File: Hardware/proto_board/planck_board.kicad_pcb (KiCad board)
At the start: 2 copper layers, 80.8 x 60.1 mm, 1 part, among them J1 Conn_01x40

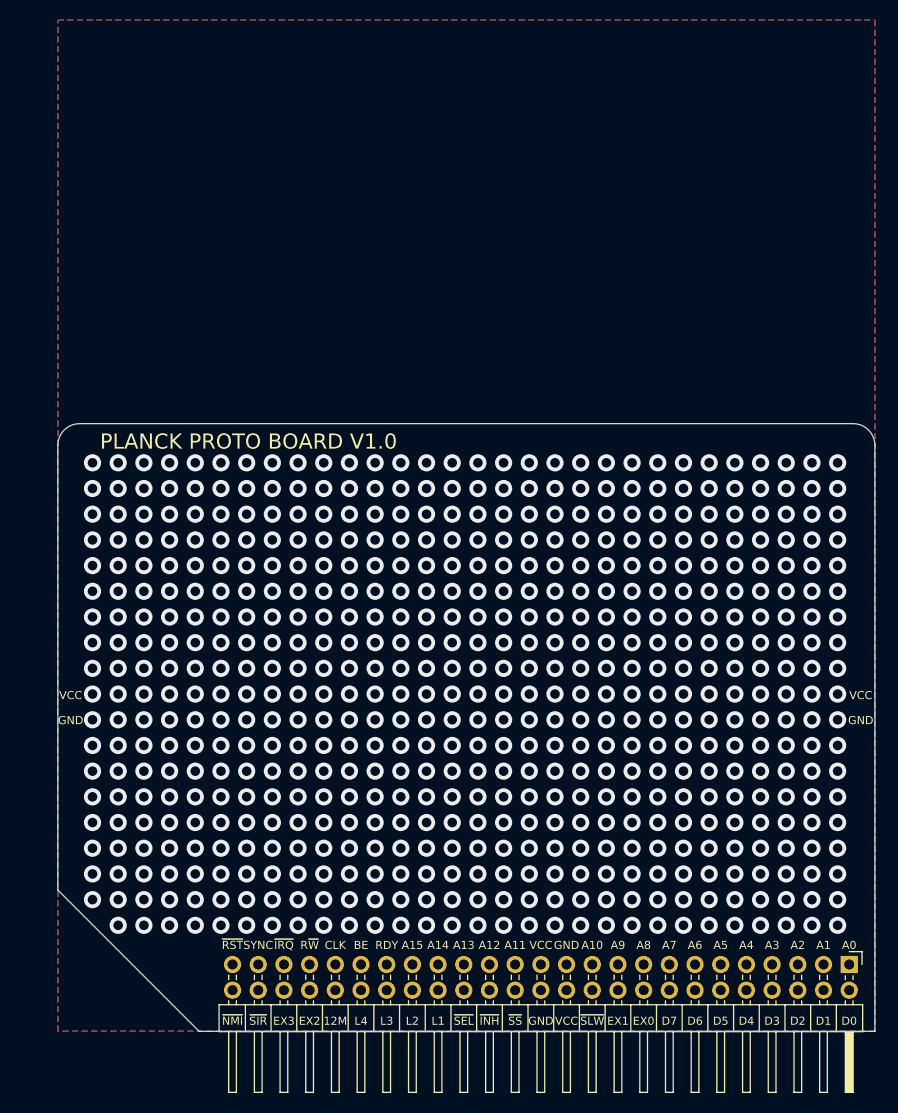
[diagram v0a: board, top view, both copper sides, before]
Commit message: update with proper pin holes
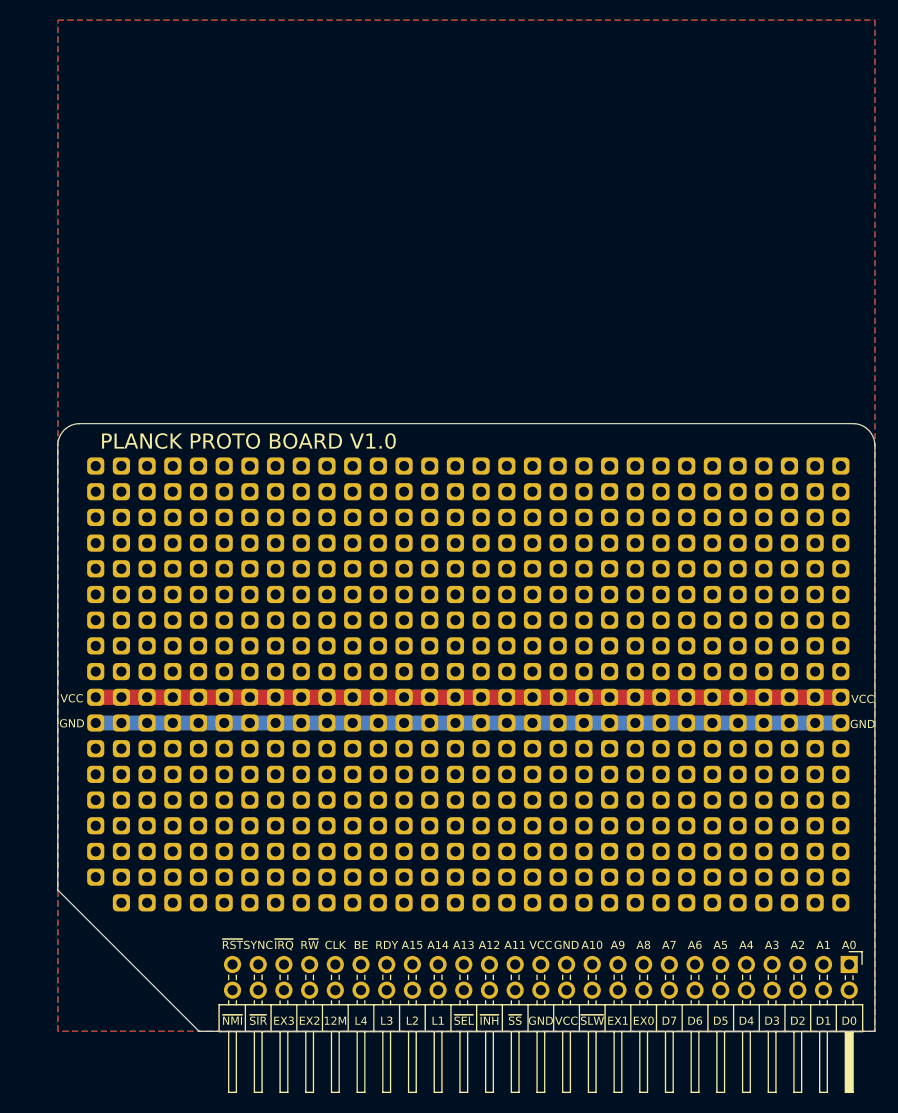
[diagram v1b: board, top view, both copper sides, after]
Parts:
- added REF**: PinHole, Connector_PinHeader_2.54mm:PinHole, F.Cu at (77.4, -33.0)
- added REF**: PinHole, Connector_PinHeader_2.54mm:PinHole, F.Cu at (54.5, -33.0)
- added REF**: PinHole, Connector_PinHeader_2.54mm:PinHole, F.Cu at (46.9, -17.8)
- added REF**: PinHole, Connector_PinHeader_2.54mm:PinHole, F.Cu at (44.4, -17.8)
- added REF**: PinHole, Connector_PinHeader_2.54mm:PinHole, F.Cu at (41.8, -17.8)
- added REF**: PinHole, Connector_PinHeader_2.54mm:PinHole, F.Cu at (39.3, -17.8)
- added REF**: PinHole, Connector_PinHeader_2.54mm:PinHole, F.Cu at (36.8, -17.8)
- added REF**: PinHole, Connector_PinHeader_2.54mm:PinHole, F.Cu at (34.2, -17.8)
- added REF**: PinHole, Connector_PinHeader_2.54mm:PinHole, F.Cu at (31.7, -17.8)
- added REF**: PinHole, Connector_PinHeader_2.54mm:PinHole, F.Cu at (29.1, -17.8)
- added REF**: PinHole, Connector_PinHeader_2.54mm:PinHole, F.Cu at (26.6, -17.8)
- added REF**: PinHole, Connector_PinHeader_2.54mm:PinHole, F.Cu at (24.1, -17.8)
- added REF**: PinHole, Connector_PinHeader_2.54mm:PinHole, F.Cu at (52.0, -33.0)
- added REF**: PinHole, Connector_PinHeader_2.54mm:PinHole, F.Cu at (21.5, -17.8)
- added REF**: PinHole, Connector_PinHeader_2.54mm:PinHole, F.Cu at (19.0, -17.8)
- added REF**: PinHole, Connector_PinHeader_2.54mm:PinHole, F.Cu at (16.4, -17.8)
- added REF**: PinHole, Connector_PinHeader_2.54mm:PinHole, F.Cu at (13.9, -17.8)
- added REF**: PinHole, Connector_PinHeader_2.54mm:PinHole, F.Cu at (11.4, -17.8)
- added REF**: PinHole, Connector_PinHeader_2.54mm:PinHole, F.Cu at (8.83, -17.8)
- added REF**: PinHole, Connector_PinHeader_2.54mm:PinHole, F.Cu at (6.29, -17.8)
- added REF**: PinHole, Connector_PinHeader_2.54mm:PinHole, F.Cu at (3.75, -17.8)
- added REF**: PinHole, Connector_PinHeader_2.54mm:PinHole, F.Cu at (77.4, -20.3)
- added REF**: PinHole, Connector_PinHeader_2.54mm:PinHole, F.Cu at (74.9, -20.3)
- added REF**: PinHole, Connector_PinHeader_2.54mm:PinHole, F.Cu at (49.5, -33.0)
- added REF**: PinHole, Connector_PinHeader_2.54mm:PinHole, F.Cu at (72.3, -20.3)
- added REF**: PinHole, Connector_PinHeader_2.54mm:PinHole, F.Cu at (69.8, -20.3)
- added REF**: PinHole, Connector_PinHeader_2.54mm:PinHole, F.Cu at (67.2, -20.3)
- added REF**: PinHole, Connector_PinHeader_2.54mm:PinHole, F.Cu at (64.7, -20.3)
- added REF**: PinHole, Connector_PinHeader_2.54mm:PinHole, F.Cu at (62.2, -20.3)
- added REF**: PinHole, Connector_PinHeader_2.54mm:PinHole, F.Cu at (59.6, -20.3)
- added REF**: PinHole, Connector_PinHeader_2.54mm:PinHole, F.Cu at (57.1, -20.3)
- added REF**: PinHole, Connector_PinHeader_2.54mm:PinHole, F.Cu at (54.5, -20.3)
- added REF**: PinHole, Connector_PinHeader_2.54mm:PinHole, F.Cu at (52.0, -20.3)
- added REF**: PinHole, Connector_PinHeader_2.54mm:PinHole, F.Cu at (49.5, -20.3)
- added REF**: PinHole, Connector_PinHeader_2.54mm:PinHole, F.Cu at (46.9, -33.0)
- added REF**: PinHole, Connector_PinHeader_2.54mm:PinHole, F.Cu at (46.9, -20.3)
- added REF**: PinHole, Connector_PinHeader_2.54mm:PinHole, F.Cu at (44.4, -20.3)
- added REF**: PinHole, Connector_PinHeader_2.54mm:PinHole, F.Cu at (41.8, -20.3)
- added REF**: PinHole, Connector_PinHeader_2.54mm:PinHole, F.Cu at (39.3, -20.3)
- added REF**: PinHole, Connector_PinHeader_2.54mm:PinHole, F.Cu at (36.8, -20.3)
- added REF**: PinHole, Connector_PinHeader_2.54mm:PinHole, F.Cu at (34.2, -20.3)
- added REF**: PinHole, Connector_PinHeader_2.54mm:PinHole, F.Cu at (31.7, -20.3)
- added REF**: PinHole, Connector_PinHeader_2.54mm:PinHole, F.Cu at (29.1, -20.3)
- added REF**: PinHole, Connector_PinHeader_2.54mm:PinHole, F.Cu at (26.6, -20.3)
- added REF**: PinHole, Connector_PinHeader_2.54mm:PinHole, F.Cu at (24.1, -20.3)
- added REF**: PinHole, Connector_PinHeader_2.54mm:PinHole, F.Cu at (44.4, -33.0)
- added REF**: PinHole, Connector_PinHeader_2.54mm:PinHole, F.Cu at (21.5, -20.3)
- added REF**: PinHole, Connector_PinHeader_2.54mm:PinHole, F.Cu at (19.0, -20.3)
- added REF**: PinHole, Connector_PinHeader_2.54mm:PinHole, F.Cu at (16.4, -20.3)
- added REF**: PinHole, Connector_PinHeader_2.54mm:PinHole, F.Cu at (13.9, -20.3)
- added REF**: PinHole, Connector_PinHeader_2.54mm:PinHole, F.Cu at (11.4, -20.3)
- added REF**: PinHole, Connector_PinHeader_2.54mm:PinHole, F.Cu at (8.83, -20.3)
- added REF**: PinHole, Connector_PinHeader_2.54mm:PinHole, F.Cu at (6.29, -20.3)
- added REF**: PinHole, Connector_PinHeader_2.54mm:PinHole, F.Cu at (3.75, -20.3)
- added REF**: PinHole, Connector_PinHeader_2.54mm:PinHole, F.Cu at (77.4, -22.9)
- added REF**: PinHole, Connector_PinHeader_2.54mm:PinHole, F.Cu at (74.9, -22.9)
- added REF**: PinHole, Connector_PinHeader_2.54mm:PinHole, F.Cu at (41.8, -33.0)
- added REF**: PinHole, Connector_PinHeader_2.54mm:PinHole, F.Cu at (72.3, -22.9)
- added REF**: PinHole, Connector_PinHeader_2.54mm:PinHole, F.Cu at (69.8, -22.9)
- added REF**: PinHole, Connector_PinHeader_2.54mm:PinHole, F.Cu at (67.2, -22.9)
- added REF**: PinHole, Connector_PinHeader_2.54mm:PinHole, F.Cu at (64.7, -22.9)
- added REF**: PinHole, Connector_PinHeader_2.54mm:PinHole, F.Cu at (62.2, -22.9)
- added REF**: PinHole, Connector_PinHeader_2.54mm:PinHole, F.Cu at (59.6, -22.9)
- added REF**: PinHole, Connector_PinHeader_2.54mm:PinHole, F.Cu at (57.1, -22.9)
- added REF**: PinHole, Connector_PinHeader_2.54mm:PinHole, F.Cu at (54.5, -22.9)
- added REF**: PinHole, Connector_PinHeader_2.54mm:PinHole, F.Cu at (52.0, -22.9)
- added REF**: PinHole, Connector_PinHeader_2.54mm:PinHole, F.Cu at (49.5, -22.9)
- added REF**: PinHole, Connector_PinHeader_2.54mm:PinHole, F.Cu at (39.3, -33.0)
- added REF**: PinHole, Connector_PinHeader_2.54mm:PinHole, F.Cu at (46.9, -22.9)
- added REF**: PinHole, Connector_PinHeader_2.54mm:PinHole, F.Cu at (44.4, -22.9)
- added REF**: PinHole, Connector_PinHeader_2.54mm:PinHole, F.Cu at (41.8, -22.9)
- added REF**: PinHole, Connector_PinHeader_2.54mm:PinHole, F.Cu at (39.3, -22.9)
- added REF**: PinHole, Connector_PinHeader_2.54mm:PinHole, F.Cu at (36.8, -22.9)
- added REF**: PinHole, Connector_PinHeader_2.54mm:PinHole, F.Cu at (34.2, -22.9)
- added REF**: PinHole, Connector_PinHeader_2.54mm:PinHole, F.Cu at (31.7, -22.9)
- added REF**: PinHole, Connector_PinHeader_2.54mm:PinHole, F.Cu at (29.1, -22.9)
- added REF**: PinHole, Connector_PinHeader_2.54mm:PinHole, F.Cu at (26.6, -22.9)
- added REF**: PinHole, Connector_PinHeader_2.54mm:PinHole, F.Cu at (24.1, -22.9)
- added REF**: PinHole, Connector_PinHeader_2.54mm:PinHole, F.Cu at (36.8, -33.0)
- added REF**: PinHole, Connector_PinHeader_2.54mm:PinHole, F.Cu at (21.5, -22.9)
- added REF**: PinHole, Connector_PinHeader_2.54mm:PinHole, F.Cu at (19.0, -22.9)
- added REF**: PinHole, Connector_PinHeader_2.54mm:PinHole, F.Cu at (16.4, -22.9)
- added REF**: PinHole, Connector_PinHeader_2.54mm:PinHole, F.Cu at (13.9, -22.9)
- added REF**: PinHole, Connector_PinHeader_2.54mm:PinHole, F.Cu at (11.4, -22.9)
- added REF**: PinHole, Connector_PinHeader_2.54mm:PinHole, F.Cu at (8.83, -22.9)
- added REF**: PinHole, Connector_PinHeader_2.54mm:PinHole, F.Cu at (6.29, -22.9)
- added REF**: PinHole, Connector_PinHeader_2.54mm:PinHole, F.Cu at (3.75, -22.9)
- added REF**: PinHole, Connector_PinHeader_2.54mm:PinHole, F.Cu at (77.4, -25.4)
- added REF**: PinHole, Connector_PinHeader_2.54mm:PinHole, F.Cu at (74.9, -25.4)
- added REF**: PinHole, Connector_PinHeader_2.54mm:PinHole, F.Cu at (34.2, -33.0)
- added REF**: PinHole, Connector_PinHeader_2.54mm:PinHole, F.Cu at (72.3, -25.4)
- added REF**: PinHole, Connector_PinHeader_2.54mm:PinHole, F.Cu at (69.8, -25.4)
- added REF**: PinHole, Connector_PinHeader_2.54mm:PinHole, F.Cu at (67.2, -25.4)
- added REF**: PinHole, Connector_PinHeader_2.54mm:PinHole, F.Cu at (64.7, -25.4)
- added REF**: PinHole, Connector_PinHeader_2.54mm:PinHole, F.Cu at (62.2, -25.4)
- added REF**: PinHole, Connector_PinHeader_2.54mm:PinHole, F.Cu at (59.6, -25.4)
- added REF**: PinHole, Connector_PinHeader_2.54mm:PinHole, F.Cu at (57.1, -25.4)
- added REF**: PinHole, Connector_PinHeader_2.54mm:PinHole, F.Cu at (54.5, -25.4)
- added REF**: PinHole, Connector_PinHeader_2.54mm:PinHole, F.Cu at (52.0, -25.4)
- added REF**: PinHole, Connector_PinHeader_2.54mm:PinHole, F.Cu at (49.5, -25.4)
- added REF**: PinHole, Connector_PinHeader_2.54mm:PinHole, F.Cu at (31.7, -33.0)
- added REF**: PinHole, Connector_PinHeader_2.54mm:PinHole, F.Cu at (46.9, -25.4)
- added REF**: PinHole, Connector_PinHeader_2.54mm:PinHole, F.Cu at (44.4, -25.4)
- added REF**: PinHole, Connector_PinHeader_2.54mm:PinHole, F.Cu at (41.8, -25.4)
- added REF**: PinHole, Connector_PinHeader_2.54mm:PinHole, F.Cu at (39.3, -25.4)
- added REF**: PinHole, Connector_PinHeader_2.54mm:PinHole, F.Cu at (36.8, -25.4)
- added REF**: PinHole, Connector_PinHeader_2.54mm:PinHole, F.Cu at (34.2, -25.4)
- added REF**: PinHole, Connector_PinHeader_2.54mm:PinHole, F.Cu at (31.7, -25.4)
- added REF**: PinHole, Connector_PinHeader_2.54mm:PinHole, F.Cu at (29.1, -25.4)
- added REF**: PinHole, Connector_PinHeader_2.54mm:PinHole, F.Cu at (26.6, -25.4)
- added REF**: PinHole, Connector_PinHeader_2.54mm:PinHole, F.Cu at (24.1, -25.4)
- added REF**: PinHole, Connector_PinHeader_2.54mm:PinHole, F.Cu at (74.9, -33.0)
- added REF**: PinHole, Connector_PinHeader_2.54mm:PinHole, F.Cu at (29.1, -33.0)
- added REF**: PinHole, Connector_PinHeader_2.54mm:PinHole, F.Cu at (21.5, -25.4)
- added REF**: PinHole, Connector_PinHeader_2.54mm:PinHole, F.Cu at (19.0, -25.4)
- added REF**: PinHole, Connector_PinHeader_2.54mm:PinHole, F.Cu at (16.4, -25.4)
- added REF**: PinHole, Connector_PinHeader_2.54mm:PinHole, F.Cu at (13.9, -25.4)
- added REF**: PinHole, Connector_PinHeader_2.54mm:PinHole, F.Cu at (11.4, -25.4)
- added REF**: PinHole, Connector_PinHeader_2.54mm:PinHole, F.Cu at (8.83, -25.4)
- added REF**: PinHole, Connector_PinHeader_2.54mm:PinHole, F.Cu at (6.29, -25.4)
- added REF**: PinHole, Connector_PinHeader_2.54mm:PinHole, F.Cu at (3.75, -25.4)
- added REF**: PinHole, Connector_PinHeader_2.54mm:PinHole, F.Cu at (77.4, -27.9)
- added REF**: PinHole, Connector_PinHeader_2.54mm:PinHole, F.Cu at (74.9, -27.9)
- added REF**: PinHole, Connector_PinHeader_2.54mm:PinHole, F.Cu at (26.6, -33.0)
- added REF**: PinHole, Connector_PinHeader_2.54mm:PinHole, F.Cu at (72.3, -27.9)
- added REF**: PinHole, Connector_PinHeader_2.54mm:PinHole, F.Cu at (69.8, -27.9)
- added REF**: PinHole, Connector_PinHeader_2.54mm:PinHole, F.Cu at (67.2, -27.9)
- added REF**: PinHole, Connector_PinHeader_2.54mm:PinHole, F.Cu at (64.7, -27.9)
- added REF**: PinHole, Connector_PinHeader_2.54mm:PinHole, F.Cu at (62.2, -27.9)
- added REF**: PinHole, Connector_PinHeader_2.54mm:PinHole, F.Cu at (59.6, -27.9)
- added REF**: PinHole, Connector_PinHeader_2.54mm:PinHole, F.Cu at (57.1, -27.9)
- added REF**: PinHole, Connector_PinHeader_2.54mm:PinHole, F.Cu at (54.5, -27.9)
- added REF**: PinHole, Connector_PinHeader_2.54mm:PinHole, F.Cu at (52.0, -27.9)
- added REF**: PinHole, Connector_PinHeader_2.54mm:PinHole, F.Cu at (49.5, -27.9)
- added REF**: PinHole, Connector_PinHeader_2.54mm:PinHole, F.Cu at (24.1, -33.0)
- added REF**: PinHole, Connector_PinHeader_2.54mm:PinHole, F.Cu at (46.9, -27.9)
- added REF**: PinHole, Connector_PinHeader_2.54mm:PinHole, F.Cu at (44.4, -27.9)
- added REF**: PinHole, Connector_PinHeader_2.54mm:PinHole, F.Cu at (41.8, -27.9)
- added REF**: PinHole, Connector_PinHeader_2.54mm:PinHole, F.Cu at (39.3, -27.9)
- added REF**: PinHole, Connector_PinHeader_2.54mm:PinHole, F.Cu at (36.8, -27.9)
- added REF**: PinHole, Connector_PinHeader_2.54mm:PinHole, F.Cu at (34.2, -27.9)
- added REF**: PinHole, Connector_PinHeader_2.54mm:PinHole, F.Cu at (31.7, -27.9)
- added REF**: PinHole, Connector_PinHeader_2.54mm:PinHole, F.Cu at (29.1, -27.9)
- added REF**: PinHole, Connector_PinHeader_2.54mm:PinHole, F.Cu at (26.6, -27.9)
- added REF**: PinHole, Connector_PinHeader_2.54mm:PinHole, F.Cu at (24.1, -27.9)
- added REF**: PinHole, Connector_PinHeader_2.54mm:PinHole, F.Cu at (21.5, -33.0)
- added REF**: PinHole, Connector_PinHeader_2.54mm:PinHole, F.Cu at (21.5, -27.9)
- added REF**: PinHole, Connector_PinHeader_2.54mm:PinHole, F.Cu at (19.0, -27.9)
- added REF**: PinHole, Connector_PinHeader_2.54mm:PinHole, F.Cu at (16.4, -27.9)
- added REF**: PinHole, Connector_PinHeader_2.54mm:PinHole, F.Cu at (13.9, -27.9)
- added REF**: PinHole, Connector_PinHeader_2.54mm:PinHole, F.Cu at (11.4, -27.9)
- added REF**: PinHole, Connector_PinHeader_2.54mm:PinHole, F.Cu at (8.83, -27.9)
- added REF**: PinHole, Connector_PinHeader_2.54mm:PinHole, F.Cu at (6.29, -27.9)
- added REF**: PinHole, Connector_PinHeader_2.54mm:PinHole, F.Cu at (3.75, -27.9)
- added REF**: PinHole, Connector_PinHeader_2.54mm:PinHole, F.Cu at (77.4, -30.5)
- added REF**: PinHole, Connector_PinHeader_2.54mm:PinHole, F.Cu at (74.9, -30.5)
- added REF**: PinHole, Connector_PinHeader_2.54mm:PinHole, F.Cu at (19.0, -33.0)
- added REF**: PinHole, Connector_PinHeader_2.54mm:PinHole, F.Cu at (72.3, -30.5)
- added REF**: PinHole, Connector_PinHeader_2.54mm:PinHole, F.Cu at (69.8, -30.5)
- added REF**: PinHole, Connector_PinHeader_2.54mm:PinHole, F.Cu at (67.2, -30.5)
- added REF**: PinHole, Connector_PinHeader_2.54mm:PinHole, F.Cu at (64.7, -30.5)
- added REF**: PinHole, Connector_PinHeader_2.54mm:PinHole, F.Cu at (62.2, -30.5)
- added REF**: PinHole, Connector_PinHeader_2.54mm:PinHole, F.Cu at (59.6, -30.5)
- added REF**: PinHole, Connector_PinHeader_2.54mm:PinHole, F.Cu at (57.1, -30.5)
- added REF**: PinHole, Connector_PinHeader_2.54mm:PinHole, F.Cu at (54.5, -30.5)
- added REF**: PinHole, Connector_PinHeader_2.54mm:PinHole, F.Cu at (52.0, -30.5)
- added REF**: PinHole, Connector_PinHeader_2.54mm:PinHole, F.Cu at (49.5, -30.5)
- added REF**: PinHole, Connector_PinHeader_2.54mm:PinHole, F.Cu at (16.4, -33.0)
- added REF**: PinHole, Connector_PinHeader_2.54mm:PinHole, F.Cu at (46.9, -30.5)
- added REF**: PinHole, Connector_PinHeader_2.54mm:PinHole, F.Cu at (44.4, -30.5)
- added REF**: PinHole, Connector_PinHeader_2.54mm:PinHole, F.Cu at (41.8, -30.5)
- added REF**: PinHole, Connector_PinHeader_2.54mm:PinHole, F.Cu at (39.3, -30.5)
- added REF**: PinHole, Connector_PinHeader_2.54mm:PinHole, F.Cu at (36.8, -30.5)
- added REF**: PinHole, Connector_PinHeader_2.54mm:PinHole, F.Cu at (34.2, -30.5)
- added REF**: PinHole, Connector_PinHeader_2.54mm:PinHole, F.Cu at (31.7, -30.5)
- added REF**: PinHole, Connector_PinHeader_2.54mm:PinHole, F.Cu at (29.1, -30.5)
- added REF**: PinHole, Connector_PinHeader_2.54mm:PinHole, F.Cu at (26.6, -30.5)
- added REF**: PinHole, Connector_PinHeader_2.54mm:PinHole, F.Cu at (24.1, -30.5)
- added REF**: PinHole, Connector_PinHeader_2.54mm:PinHole, F.Cu at (13.9, -33.0)
- added REF**: PinHole, Connector_PinHeader_2.54mm:PinHole, F.Cu at (21.5, -30.5)
- added REF**: PinHole, Connector_PinHeader_2.54mm:PinHole, F.Cu at (19.0, -30.5)
- added REF**: PinHole, Connector_PinHeader_2.54mm:PinHole, F.Cu at (16.4, -30.5)
- added REF**: PinHole, Connector_PinHeader_2.54mm:PinHole, F.Cu at (13.9, -30.5)
- added REF**: PinHole, Connector_PinHeader_2.54mm:PinHole, F.Cu at (11.4, -30.5)
- added REF**: PinHole, Connector_PinHeader_2.54mm:PinHole, F.Cu at (8.83, -30.5)
- added REF**: PinHole, Connector_PinHeader_2.54mm:PinHole, F.Cu at (6.29, -30.5)
- added REF**: PinHole, Connector_PinHeader_2.54mm:PinHole, F.Cu at (3.75, -30.5)
- added REF**: PinHole, Connector_PinHeader_2.54mm:PinHole, F.Cu at (3.75, -33.0)
- added REF**: PinHole, Connector_PinHeader_2.54mm:PinHole, F.Cu at (3.75, -35.6)
- added REF**: PinHole, Connector_PinHeader_2.54mm:PinHole, F.Cu at (11.4, -33.0)
- added REF**: PinHole, Connector_PinHeader_2.54mm:PinHole, F.Cu at (77.4, -38.1)
- added REF**: PinHole, Connector_PinHeader_2.54mm:PinHole, F.Cu at (74.9, -38.1)
- added REF**: PinHole, Connector_PinHeader_2.54mm:PinHole, F.Cu at (72.3, -38.1)
- added REF**: PinHole, Connector_PinHeader_2.54mm:PinHole, F.Cu at (69.8, -38.1)
- added REF**: PinHole, Connector_PinHeader_2.54mm:PinHole, F.Cu at (67.2, -38.1)
- added REF**: PinHole, Connector_PinHeader_2.54mm:PinHole, F.Cu at (64.7, -38.1)
- added REF**: PinHole, Connector_PinHeader_2.54mm:PinHole, F.Cu at (62.2, -38.1)
- added REF**: PinHole, Connector_PinHeader_2.54mm:PinHole, F.Cu at (59.6, -38.1)
- added REF**: PinHole, Connector_PinHeader_2.54mm:PinHole, F.Cu at (57.1, -38.1)
- added REF**: PinHole, Connector_PinHeader_2.54mm:PinHole, F.Cu at (54.5, -38.1)
- added REF**: PinHole, Connector_PinHeader_2.54mm:PinHole, F.Cu at (8.83, -33.0)
- added REF**: PinHole, Connector_PinHeader_2.54mm:PinHole, F.Cu at (52.0, -38.1)
- added REF**: PinHole, Connector_PinHeader_2.54mm:PinHole, F.Cu at (49.5, -38.1)
- added REF**: PinHole, Connector_PinHeader_2.54mm:PinHole, F.Cu at (46.9, -38.1)
- added REF**: PinHole, Connector_PinHeader_2.54mm:PinHole, F.Cu at (44.4, -38.1)
- added REF**: PinHole, Connector_PinHeader_2.54mm:PinHole, F.Cu at (41.8, -38.1)
- added REF**: PinHole, Connector_PinHeader_2.54mm:PinHole, F.Cu at (39.3, -38.1)
- added REF**: PinHole, Connector_PinHeader_2.54mm:PinHole, F.Cu at (36.8, -38.1)
- added REF**: PinHole, Connector_PinHeader_2.54mm:PinHole, F.Cu at (34.2, -38.1)
- added REF**: PinHole, Connector_PinHeader_2.54mm:PinHole, F.Cu at (31.7, -38.1)
- added REF**: PinHole, Connector_PinHeader_2.54mm:PinHole, F.Cu at (29.1, -38.1)
- added REF**: PinHole, Connector_PinHeader_2.54mm:PinHole, F.Cu at (6.29, -33.0)
- added REF**: PinHole, Connector_PinHeader_2.54mm:PinHole, F.Cu at (26.6, -38.1)
- added REF**: PinHole, Connector_PinHeader_2.54mm:PinHole, F.Cu at (24.1, -38.1)
- added REF**: PinHole, Connector_PinHeader_2.54mm:PinHole, F.Cu at (21.5, -38.1)
- added REF**: PinHole, Connector_PinHeader_2.54mm:PinHole, F.Cu at (19.0, -38.1)
- added REF**: PinHole, Connector_PinHeader_2.54mm:PinHole, F.Cu at (16.4, -38.1)
- added REF**: PinHole, Connector_PinHeader_2.54mm:PinHole, F.Cu at (13.9, -38.1)
- added REF**: PinHole, Connector_PinHeader_2.54mm:PinHole, F.Cu at (11.4, -38.1)
- added REF**: PinHole, Connector_PinHeader_2.54mm:PinHole, F.Cu at (8.83, -38.1)
- added REF**: PinHole, Connector_PinHeader_2.54mm:PinHole, F.Cu at (6.29, -38.1)
- added REF**: PinHole, Connector_PinHeader_2.54mm:PinHole, F.Cu at (3.75, -38.1)
- added REF**: PinHole, Connector_PinHeader_2.54mm:PinHole, F.Cu at (72.3, -33.0)
- added REF**: PinHole, Connector_PinHeader_2.54mm:PinHole, F.Cu at (77.4, -35.6)
- added REF**: PinHole, Connector_PinHeader_2.54mm:PinHole, F.Cu at (77.4, -40.6)
- added REF**: PinHole, Connector_PinHeader_2.54mm:PinHole, F.Cu at (74.9, -40.6)
- added REF**: PinHole, Connector_PinHeader_2.54mm:PinHole, F.Cu at (72.3, -40.6)
- added REF**: PinHole, Connector_PinHeader_2.54mm:PinHole, F.Cu at (69.8, -40.6)
- added REF**: PinHole, Connector_PinHeader_2.54mm:PinHole, F.Cu at (67.2, -40.6)
- added REF**: PinHole, Connector_PinHeader_2.54mm:PinHole, F.Cu at (64.7, -40.6)
- added REF**: PinHole, Connector_PinHeader_2.54mm:PinHole, F.Cu at (62.2, -40.6)
- added REF**: PinHole, Connector_PinHeader_2.54mm:PinHole, F.Cu at (59.6, -40.6)
- added REF**: PinHole, Connector_PinHeader_2.54mm:PinHole, F.Cu at (57.1, -40.6)
- added REF**: PinHole, Connector_PinHeader_2.54mm:PinHole, F.Cu at (54.5, -40.6)
- added REF**: PinHole, Connector_PinHeader_2.54mm:PinHole, F.Cu at (74.9, -35.6)
- added REF**: PinHole, Connector_PinHeader_2.54mm:PinHole, F.Cu at (52.0, -40.6)
- added REF**: PinHole, Connector_PinHeader_2.54mm:PinHole, F.Cu at (49.5, -40.6)
- added REF**: PinHole, Connector_PinHeader_2.54mm:PinHole, F.Cu at (46.9, -40.6)
- added REF**: PinHole, Connector_PinHeader_2.54mm:PinHole, F.Cu at (44.4, -40.6)
- added REF**: PinHole, Connector_PinHeader_2.54mm:PinHole, F.Cu at (41.8, -40.6)
- added REF**: PinHole, Connector_PinHeader_2.54mm:PinHole, F.Cu at (39.3, -40.6)
- added REF**: PinHole, Connector_PinHeader_2.54mm:PinHole, F.Cu at (36.8, -40.6)
- added REF**: PinHole, Connector_PinHeader_2.54mm:PinHole, F.Cu at (34.2, -40.6)
- added REF**: PinHole, Connector_PinHeader_2.54mm:PinHole, F.Cu at (31.7, -40.6)
- added REF**: PinHole, Connector_PinHeader_2.54mm:PinHole, F.Cu at (29.1, -40.6)
- added REF**: PinHole, Connector_PinHeader_2.54mm:PinHole, F.Cu at (72.3, -35.6)
- added REF**: PinHole, Connector_PinHeader_2.54mm:PinHole, F.Cu at (26.6, -40.6)
- added REF**: PinHole, Connector_PinHeader_2.54mm:PinHole, F.Cu at (24.1, -40.6)
- added REF**: PinHole, Connector_PinHeader_2.54mm:PinHole, F.Cu at (21.5, -40.6)
- added REF**: PinHole, Connector_PinHeader_2.54mm:PinHole, F.Cu at (19.0, -40.6)
- added REF**: PinHole, Connector_PinHeader_2.54mm:PinHole, F.Cu at (16.4, -40.6)
- added REF**: PinHole, Connector_PinHeader_2.54mm:PinHole, F.Cu at (13.9, -40.6)
- added REF**: PinHole, Connector_PinHeader_2.54mm:PinHole, F.Cu at (11.4, -40.6)
- added REF**: PinHole, Connector_PinHeader_2.54mm:PinHole, F.Cu at (8.83, -40.6)
- added REF**: PinHole, Connector_PinHeader_2.54mm:PinHole, F.Cu at (6.29, -40.6)
- added REF**: PinHole, Connector_PinHeader_2.54mm:PinHole, F.Cu at (3.75, -40.6)
- added REF**: PinHole, Connector_PinHeader_2.54mm:PinHole, F.Cu at (69.8, -35.6)
- added REF**: PinHole, Connector_PinHeader_2.54mm:PinHole, F.Cu at (77.4, -43.2)
- added REF**: PinHole, Connector_PinHeader_2.54mm:PinHole, F.Cu at (74.9, -43.2)
- added REF**: PinHole, Connector_PinHeader_2.54mm:PinHole, F.Cu at (72.3, -43.2)
- added REF**: PinHole, Connector_PinHeader_2.54mm:PinHole, F.Cu at (69.8, -43.2)
- added REF**: PinHole, Connector_PinHeader_2.54mm:PinHole, F.Cu at (67.2, -43.2)
- added REF**: PinHole, Connector_PinHeader_2.54mm:PinHole, F.Cu at (64.7, -43.2)
- added REF**: PinHole, Connector_PinHeader_2.54mm:PinHole, F.Cu at (62.2, -43.2)
- added REF**: PinHole, Connector_PinHeader_2.54mm:PinHole, F.Cu at (59.6, -43.2)
- added REF**: PinHole, Connector_PinHeader_2.54mm:PinHole, F.Cu at (57.1, -43.2)
- added REF**: PinHole, Connector_PinHeader_2.54mm:PinHole, F.Cu at (54.5, -43.2)
- added REF**: PinHole, Connector_PinHeader_2.54mm:PinHole, F.Cu at (67.2, -35.6)
- added REF**: PinHole, Connector_PinHeader_2.54mm:PinHole, F.Cu at (52.0, -43.2)
- added REF**: PinHole, Connector_PinHeader_2.54mm:PinHole, F.Cu at (49.5, -43.2)
- added REF**: PinHole, Connector_PinHeader_2.54mm:PinHole, F.Cu at (46.9, -43.2)
- added REF**: PinHole, Connector_PinHeader_2.54mm:PinHole, F.Cu at (44.4, -43.2)
- added REF**: PinHole, Connector_PinHeader_2.54mm:PinHole, F.Cu at (41.8, -43.2)
- added REF**: PinHole, Connector_PinHeader_2.54mm:PinHole, F.Cu at (39.3, -43.2)
- added REF**: PinHole, Connector_PinHeader_2.54mm:PinHole, F.Cu at (36.8, -43.2)
- added REF**: PinHole, Connector_PinHeader_2.54mm:PinHole, F.Cu at (34.2, -43.2)
- added REF**: PinHole, Connector_PinHeader_2.54mm:PinHole, F.Cu at (31.7, -43.2)
- added REF**: PinHole, Connector_PinHeader_2.54mm:PinHole, F.Cu at (29.1, -43.2)
- added REF**: PinHole, Connector_PinHeader_2.54mm:PinHole, F.Cu at (64.7, -35.6)
- added REF**: PinHole, Connector_PinHeader_2.54mm:PinHole, F.Cu at (26.6, -43.2)
- added REF**: PinHole, Connector_PinHeader_2.54mm:PinHole, F.Cu at (24.1, -43.2)
- added REF**: PinHole, Connector_PinHeader_2.54mm:PinHole, F.Cu at (21.5, -43.2)
- added REF**: PinHole, Connector_PinHeader_2.54mm:PinHole, F.Cu at (19.0, -43.2)
- added REF**: PinHole, Connector_PinHeader_2.54mm:PinHole, F.Cu at (16.4, -43.2)
- added REF**: PinHole, Connector_PinHeader_2.54mm:PinHole, F.Cu at (13.9, -43.2)
- added REF**: PinHole, Connector_PinHeader_2.54mm:PinHole, F.Cu at (11.4, -43.2)
- added REF**: PinHole, Connector_PinHeader_2.54mm:PinHole, F.Cu at (8.83, -43.2)
- added REF**: PinHole, Connector_PinHeader_2.54mm:PinHole, F.Cu at (6.29, -43.2)
- added REF**: PinHole, Connector_PinHeader_2.54mm:PinHole, F.Cu at (3.75, -43.2)
- added REF**: PinHole, Connector_PinHeader_2.54mm:PinHole, F.Cu at (62.2, -35.6)
- added REF**: PinHole, Connector_PinHeader_2.54mm:PinHole, F.Cu at (77.4, -45.7)
- added REF**: PinHole, Connector_PinHeader_2.54mm:PinHole, F.Cu at (74.9, -45.7)
- added REF**: PinHole, Connector_PinHeader_2.54mm:PinHole, F.Cu at (72.3, -45.7)
- added REF**: PinHole, Connector_PinHeader_2.54mm:PinHole, F.Cu at (69.8, -45.7)
- added REF**: PinHole, Connector_PinHeader_2.54mm:PinHole, F.Cu at (67.2, -45.7)
- added REF**: PinHole, Connector_PinHeader_2.54mm:PinHole, F.Cu at (64.7, -45.7)
- added REF**: PinHole, Connector_PinHeader_2.54mm:PinHole, F.Cu at (62.2, -45.7)
- added REF**: PinHole, Connector_PinHeader_2.54mm:PinHole, F.Cu at (59.6, -45.7)
- added REF**: PinHole, Connector_PinHeader_2.54mm:PinHole, F.Cu at (57.1, -45.7)
- added REF**: PinHole, Connector_PinHeader_2.54mm:PinHole, F.Cu at (54.5, -45.7)
- added REF**: PinHole, Connector_PinHeader_2.54mm:PinHole, F.Cu at (59.6, -35.6)
- added REF**: PinHole, Connector_PinHeader_2.54mm:PinHole, F.Cu at (52.0, -45.7)
- added REF**: PinHole, Connector_PinHeader_2.54mm:PinHole, F.Cu at (49.5, -45.7)
- added REF**: PinHole, Connector_PinHeader_2.54mm:PinHole, F.Cu at (46.9, -45.7)
- added REF**: PinHole, Connector_PinHeader_2.54mm:PinHole, F.Cu at (44.4, -45.7)
- added REF**: PinHole, Connector_PinHeader_2.54mm:PinHole, F.Cu at (41.8, -45.7)
- added REF**: PinHole, Connector_PinHeader_2.54mm:PinHole, F.Cu at (39.3, -45.7)
- added REF**: PinHole, Connector_PinHeader_2.54mm:PinHole, F.Cu at (36.8, -45.7)
- added REF**: PinHole, Connector_PinHeader_2.54mm:PinHole, F.Cu at (34.2, -45.7)
- added REF**: PinHole, Connector_PinHeader_2.54mm:PinHole, F.Cu at (31.7, -45.7)
- added REF**: PinHole, Connector_PinHeader_2.54mm:PinHole, F.Cu at (29.1, -45.7)
- added REF**: PinHole, Connector_PinHeader_2.54mm:PinHole, F.Cu at (57.1, -35.6)
- added REF**: PinHole, Connector_PinHeader_2.54mm:PinHole, F.Cu at (26.6, -45.7)
- added REF**: PinHole, Connector_PinHeader_2.54mm:PinHole, F.Cu at (24.1, -45.7)
- added REF**: PinHole, Connector_PinHeader_2.54mm:PinHole, F.Cu at (21.5, -45.7)
- added REF**: PinHole, Connector_PinHeader_2.54mm:PinHole, F.Cu at (19.0, -45.7)
- added REF**: PinHole, Connector_PinHeader_2.54mm:PinHole, F.Cu at (16.4, -45.7)
- added REF**: PinHole, Connector_PinHeader_2.54mm:PinHole, F.Cu at (13.9, -45.7)
- added REF**: PinHole, Connector_PinHeader_2.54mm:PinHole, F.Cu at (11.4, -45.7)
- added REF**: PinHole, Connector_PinHeader_2.54mm:PinHole, F.Cu at (8.83, -45.7)
- added REF**: PinHole, Connector_PinHeader_2.54mm:PinHole, F.Cu at (6.29, -45.7)
- added REF**: PinHole, Connector_PinHeader_2.54mm:PinHole, F.Cu at (3.75, -45.7)
- added REF**: PinHole, Connector_PinHeader_2.54mm:PinHole, F.Cu at (54.5, -35.6)
- added REF**: PinHole, Connector_PinHeader_2.54mm:PinHole, F.Cu at (77.4, -48.3)
- added REF**: PinHole, Connector_PinHeader_2.54mm:PinHole, F.Cu at (74.9, -48.3)
- added REF**: PinHole, Connector_PinHeader_2.54mm:PinHole, F.Cu at (72.3, -48.3)
- added REF**: PinHole, Connector_PinHeader_2.54mm:PinHole, F.Cu at (69.8, -48.3)
- added REF**: PinHole, Connector_PinHeader_2.54mm:PinHole, F.Cu at (67.2, -48.3)
- added REF**: PinHole, Connector_PinHeader_2.54mm:PinHole, F.Cu at (64.7, -48.3)
- added REF**: PinHole, Connector_PinHeader_2.54mm:PinHole, F.Cu at (62.2, -48.3)
- added REF**: PinHole, Connector_PinHeader_2.54mm:PinHole, F.Cu at (59.6, -48.3)
- added REF**: PinHole, Connector_PinHeader_2.54mm:PinHole, F.Cu at (57.1, -48.3)
- added REF**: PinHole, Connector_PinHeader_2.54mm:PinHole, F.Cu at (54.5, -48.3)
- added REF**: PinHole, Connector_PinHeader_2.54mm:PinHole, F.Cu at (69.8, -33.0)
- added REF**: PinHole, Connector_PinHeader_2.54mm:PinHole, F.Cu at (52.0, -35.6)
- added REF**: PinHole, Connector_PinHeader_2.54mm:PinHole, F.Cu at (52.0, -48.3)
- added REF**: PinHole, Connector_PinHeader_2.54mm:PinHole, F.Cu at (49.5, -48.3)
- added REF**: PinHole, Connector_PinHeader_2.54mm:PinHole, F.Cu at (46.9, -48.3)
- added REF**: PinHole, Connector_PinHeader_2.54mm:PinHole, F.Cu at (44.4, -48.3)
- added REF**: PinHole, Connector_PinHeader_2.54mm:PinHole, F.Cu at (41.8, -48.3)
- added REF**: PinHole, Connector_PinHeader_2.54mm:PinHole, F.Cu at (39.3, -48.3)
- added REF**: PinHole, Connector_PinHeader_2.54mm:PinHole, F.Cu at (36.8, -48.3)
- added REF**: PinHole, Connector_PinHeader_2.54mm:PinHole, F.Cu at (34.2, -48.3)
- added REF**: PinHole, Connector_PinHeader_2.54mm:PinHole, F.Cu at (31.7, -48.3)
- added REF**: PinHole, Connector_PinHeader_2.54mm:PinHole, F.Cu at (29.1, -48.3)
- added REF**: PinHole, Connector_PinHeader_2.54mm:PinHole, F.Cu at (49.5, -35.6)
- added REF**: PinHole, Connector_PinHeader_2.54mm:PinHole, F.Cu at (26.6, -48.3)
- added REF**: PinHole, Connector_PinHeader_2.54mm:PinHole, F.Cu at (24.1, -48.3)
- added REF**: PinHole, Connector_PinHeader_2.54mm:PinHole, F.Cu at (21.5, -48.3)
- added REF**: PinHole, Connector_PinHeader_2.54mm:PinHole, F.Cu at (19.0, -48.3)
- added REF**: PinHole, Connector_PinHeader_2.54mm:PinHole, F.Cu at (16.4, -48.3)
- added REF**: PinHole, Connector_PinHeader_2.54mm:PinHole, F.Cu at (13.9, -48.3)
- added REF**: PinHole, Connector_PinHeader_2.54mm:PinHole, F.Cu at (11.4, -48.3)
- added REF**: PinHole, Connector_PinHeader_2.54mm:PinHole, F.Cu at (8.83, -48.3)
- added REF**: PinHole, Connector_PinHeader_2.54mm:PinHole, F.Cu at (6.29, -48.3)
- added REF**: PinHole, Connector_PinHeader_2.54mm:PinHole, F.Cu at (3.75, -48.3)
- added REF**: PinHole, Connector_PinHeader_2.54mm:PinHole, F.Cu at (46.9, -35.6)
- added REF**: PinHole, Connector_PinHeader_2.54mm:PinHole, F.Cu at (77.4, -50.8)
- added REF**: PinHole, Connector_PinHeader_2.54mm:PinHole, F.Cu at (74.9, -50.8)
- added REF**: PinHole, Connector_PinHeader_2.54mm:PinHole, F.Cu at (72.3, -50.8)
- added REF**: PinHole, Connector_PinHeader_2.54mm:PinHole, F.Cu at (69.8, -50.8)
- added REF**: PinHole, Connector_PinHeader_2.54mm:PinHole, F.Cu at (67.2, -50.8)
- added REF**: PinHole, Connector_PinHeader_2.54mm:PinHole, F.Cu at (64.7, -50.8)
- added REF**: PinHole, Connector_PinHeader_2.54mm:PinHole, F.Cu at (62.2, -50.8)
- added REF**: PinHole, Connector_PinHeader_2.54mm:PinHole, F.Cu at (59.6, -50.8)
- added REF**: PinHole, Connector_PinHeader_2.54mm:PinHole, F.Cu at (57.1, -50.8)
- added REF**: PinHole, Connector_PinHeader_2.54mm:PinHole, F.Cu at (54.5, -50.8)
- added REF**: PinHole, Connector_PinHeader_2.54mm:PinHole, F.Cu at (44.4, -35.6)
- added REF**: PinHole, Connector_PinHeader_2.54mm:PinHole, F.Cu at (52.0, -50.8)
- added REF**: PinHole, Connector_PinHeader_2.54mm:PinHole, F.Cu at (49.5, -50.8)
- added REF**: PinHole, Connector_PinHeader_2.54mm:PinHole, F.Cu at (46.9, -50.8)
- added REF**: PinHole, Connector_PinHeader_2.54mm:PinHole, F.Cu at (44.4, -50.8)
- added REF**: PinHole, Connector_PinHeader_2.54mm:PinHole, F.Cu at (41.8, -50.8)
- added REF**: PinHole, Connector_PinHeader_2.54mm:PinHole, F.Cu at (39.3, -50.8)
- added REF**: PinHole, Connector_PinHeader_2.54mm:PinHole, F.Cu at (36.8, -50.8)
- added REF**: PinHole, Connector_PinHeader_2.54mm:PinHole, F.Cu at (34.2, -50.8)
- added REF**: PinHole, Connector_PinHeader_2.54mm:PinHole, F.Cu at (31.7, -50.8)
- added REF**: PinHole, Connector_PinHeader_2.54mm:PinHole, F.Cu at (29.1, -50.8)
- added REF**: PinHole, Connector_PinHeader_2.54mm:PinHole, F.Cu at (41.8, -35.6)
- added REF**: PinHole, Connector_PinHeader_2.54mm:PinHole, F.Cu at (26.6, -50.8)
- added REF**: PinHole, Connector_PinHeader_2.54mm:PinHole, F.Cu at (24.1, -50.8)
- added REF**: PinHole, Connector_PinHeader_2.54mm:PinHole, F.Cu at (21.5, -50.8)
- added REF**: PinHole, Connector_PinHeader_2.54mm:PinHole, F.Cu at (19.0, -50.8)
- added REF**: PinHole, Connector_PinHeader_2.54mm:PinHole, F.Cu at (16.4, -50.8)
- added REF**: PinHole, Connector_PinHeader_2.54mm:PinHole, F.Cu at (13.9, -50.8)
- added REF**: PinHole, Connector_PinHeader_2.54mm:PinHole, F.Cu at (11.4, -50.8)
- added REF**: PinHole, Connector_PinHeader_2.54mm:PinHole, F.Cu at (8.83, -50.8)
- added REF**: PinHole, Connector_PinHeader_2.54mm:PinHole, F.Cu at (6.29, -50.8)
- added REF**: PinHole, Connector_PinHeader_2.54mm:PinHole, F.Cu at (3.75, -50.8)
- added REF**: PinHole, Connector_PinHeader_2.54mm:PinHole, F.Cu at (39.3, -35.6)
- added REF**: PinHole, Connector_PinHeader_2.54mm:PinHole, F.Cu at (77.4, -53.3)
- added REF**: PinHole, Connector_PinHeader_2.54mm:PinHole, F.Cu at (74.9, -53.3)
- added REF**: PinHole, Connector_PinHeader_2.54mm:PinHole, F.Cu at (72.3, -53.3)
- added REF**: PinHole, Connector_PinHeader_2.54mm:PinHole, F.Cu at (69.8, -53.3)
- added REF**: PinHole, Connector_PinHeader_2.54mm:PinHole, F.Cu at (67.2, -53.3)
- added REF**: PinHole, Connector_PinHeader_2.54mm:PinHole, F.Cu at (64.7, -53.3)
- added REF**: PinHole, Connector_PinHeader_2.54mm:PinHole, F.Cu at (62.2, -53.3)
- added REF**: PinHole, Connector_PinHeader_2.54mm:PinHole, F.Cu at (59.6, -53.3)
- added REF**: PinHole, Connector_PinHeader_2.54mm:PinHole, F.Cu at (57.1, -53.3)
- added REF**: PinHole, Connector_PinHeader_2.54mm:PinHole, F.Cu at (54.5, -53.3)
- added REF**: PinHole, Connector_PinHeader_2.54mm:PinHole, F.Cu at (36.8, -35.6)
- added REF**: PinHole, Connector_PinHeader_2.54mm:PinHole, F.Cu at (52.0, -53.3)
- added REF**: PinHole, Connector_PinHeader_2.54mm:PinHole, F.Cu at (49.5, -53.3)
- added REF**: PinHole, Connector_PinHeader_2.54mm:PinHole, F.Cu at (46.9, -53.3)
- added REF**: PinHole, Connector_PinHeader_2.54mm:PinHole, F.Cu at (44.4, -53.3)
- added REF**: PinHole, Connector_PinHeader_2.54mm:PinHole, F.Cu at (41.8, -53.3)
- added REF**: PinHole, Connector_PinHeader_2.54mm:PinHole, F.Cu at (39.3, -53.3)
- added REF**: PinHole, Connector_PinHeader_2.54mm:PinHole, F.Cu at (36.8, -53.3)
- added REF**: PinHole, Connector_PinHeader_2.54mm:PinHole, F.Cu at (34.2, -53.3)
- added REF**: PinHole, Connector_PinHeader_2.54mm:PinHole, F.Cu at (31.7, -53.3)
- added REF**: PinHole, Connector_PinHeader_2.54mm:PinHole, F.Cu at (29.1, -53.3)
- added REF**: PinHole, Connector_PinHeader_2.54mm:PinHole, F.Cu at (34.2, -35.6)
- added REF**: PinHole, Connector_PinHeader_2.54mm:PinHole, F.Cu at (26.6, -53.3)
- added REF**: PinHole, Connector_PinHeader_2.54mm:PinHole, F.Cu at (24.1, -53.3)
- added REF**: PinHole, Connector_PinHeader_2.54mm:PinHole, F.Cu at (21.5, -53.3)
- added REF**: PinHole, Connector_PinHeader_2.54mm:PinHole, F.Cu at (19.0, -53.3)
- added REF**: PinHole, Connector_PinHeader_2.54mm:PinHole, F.Cu at (16.4, -53.3)
- added REF**: PinHole, Connector_PinHeader_2.54mm:PinHole, F.Cu at (13.9, -53.3)
- added REF**: PinHole, Connector_PinHeader_2.54mm:PinHole, F.Cu at (11.4, -53.3)
- added REF**: PinHole, Connector_PinHeader_2.54mm:PinHole, F.Cu at (8.83, -53.3)
- added REF**: PinHole, Connector_PinHeader_2.54mm:PinHole, F.Cu at (6.29, -53.3)
- added REF**: PinHole, Connector_PinHeader_2.54mm:PinHole, F.Cu at (3.75, -53.3)
- added REF**: PinHole, Connector_PinHeader_2.54mm:PinHole, F.Cu at (31.7, -35.6)
- added REF**: PinHole, Connector_PinHeader_2.54mm:PinHole, F.Cu at (77.4, -55.9)
- added REF**: PinHole, Connector_PinHeader_2.54mm:PinHole, F.Cu at (74.9, -55.9)
- added REF**: PinHole, Connector_PinHeader_2.54mm:PinHole, F.Cu at (72.3, -55.9)
- added REF**: PinHole, Connector_PinHeader_2.54mm:PinHole, F.Cu at (69.8, -55.9)
- added REF**: PinHole, Connector_PinHeader_2.54mm:PinHole, F.Cu at (67.2, -55.9)
- added REF**: PinHole, Connector_PinHeader_2.54mm:PinHole, F.Cu at (64.7, -55.9)
- added REF**: PinHole, Connector_PinHeader_2.54mm:PinHole, F.Cu at (62.2, -55.9)
- added REF**: PinHole, Connector_PinHeader_2.54mm:PinHole, F.Cu at (59.6, -55.9)
- added REF**: PinHole, Connector_PinHeader_2.54mm:PinHole, F.Cu at (57.1, -55.9)
- added REF**: PinHole, Connector_PinHeader_2.54mm:PinHole, F.Cu at (54.5, -55.9)
- added REF**: PinHole, Connector_PinHeader_2.54mm:PinHole, F.Cu at (29.1, -35.6)
- added REF**: PinHole, Connector_PinHeader_2.54mm:PinHole, F.Cu at (52.0, -55.9)
- added REF**: PinHole, Connector_PinHeader_2.54mm:PinHole, F.Cu at (49.5, -55.9)
- added REF**: PinHole, Connector_PinHeader_2.54mm:PinHole, F.Cu at (46.9, -55.9)
- added REF**: PinHole, Connector_PinHeader_2.54mm:PinHole, F.Cu at (44.4, -55.9)
- added REF**: PinHole, Connector_PinHeader_2.54mm:PinHole, F.Cu at (41.8, -55.9)
- added REF**: PinHole, Connector_PinHeader_2.54mm:PinHole, F.Cu at (39.3, -55.9)
- added REF**: PinHole, Connector_PinHeader_2.54mm:PinHole, F.Cu at (36.8, -55.9)
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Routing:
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
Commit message: Add silkscreen on back of prototype board
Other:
- rule pad_to_mask_clearance: 0.05 -> 0

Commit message: update for kicad 6
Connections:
- net R~W~ renamed R~{W}
- net ~INH~ renamed ~{INH}
- net ~IRQ~ renamed ~{IRQ}
- net ~NMI~ renamed ~{NMI}
- net ~RESET~ renamed ~{RESET}
- net ~SLOT_IRQ~ renamed ~{SLOT_IRQ}
- net ~SLOT_SEL~ renamed ~{SLOT_SEL}
- net ~SLOW~ renamed ~{SLOW}
- net ~SSEL~ renamed ~{SSEL}
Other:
- net class Default removed
- board text added: "PLANCK PROTO BOARD ${VERSION}"
- board text added: "R~{W}"
- board text added: "~{INH}"
- board text added: "~{IRQ}"
- board text added: "~{NMI}"
- board text added: "~{RST}"
- board text added: "~{SEL}"
- board text added: "~{SIR}"
- board text added: "~{SLW}"
- board text added: "~{SS}"
- board text removed: "PLANCK PROTO BOARD V1.0"
- board text removed: "R~W~"
- board text removed: "~INH~"
- board text removed: "~IRQ~"
- board text removed: "~NMI~"
- board text removed: "~RST~"
- board text removed: "~SEL~"
- board text removed: "~SIR~"
- board text removed: "~SLW~"
- board text removed: "~SS~"
